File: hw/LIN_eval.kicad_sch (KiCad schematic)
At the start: 44 parts, among them J1 STM32 SWD, J2 Conn_01x03, Q2 DMG1012T, Q3 DMG1012T, Q4 DMG1012T, U1 TJA1029TK, U2 AP7370-33FDC, U3 STM32G030K8Tx, U4 DS18B20, Y2 8Mhz

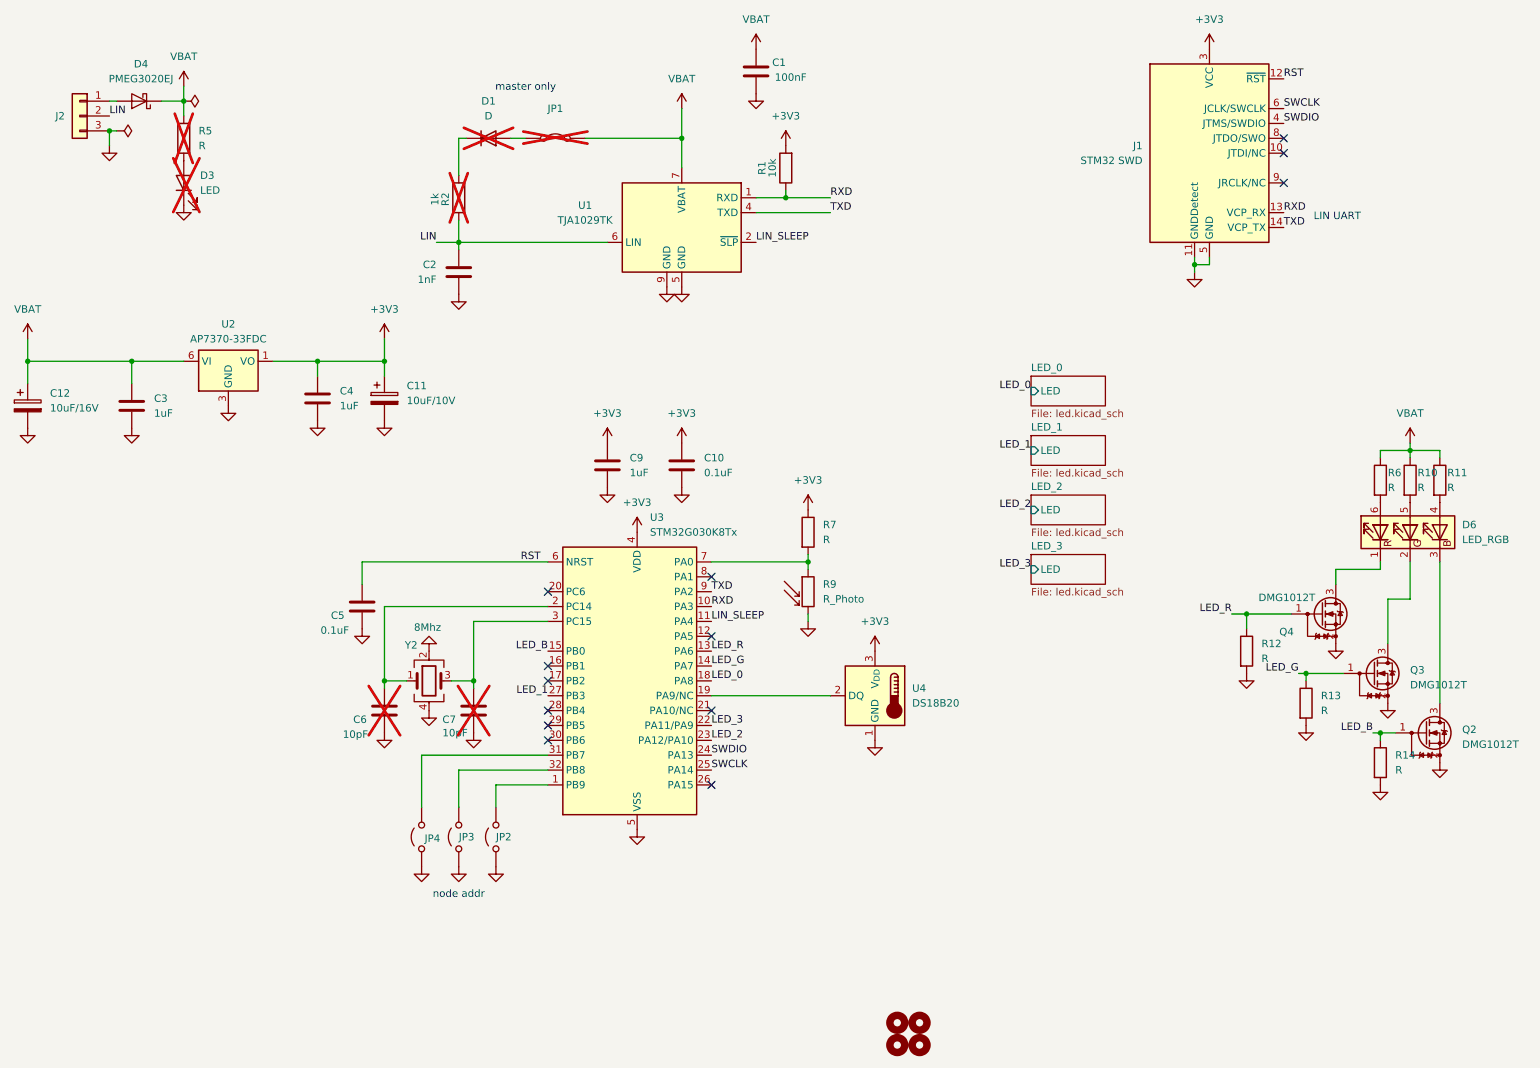
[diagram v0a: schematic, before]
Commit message: hw: version v2 with improvements
- removed LIN UART RX/TX from debugger connector as it drives signal from two sources
- added 5k pull-up to DS18B20 1-Wire bus
- added 1.27mm connector for additional devices on 1-Wire bus
- shifted address jumpers little bit farther from debugger connector
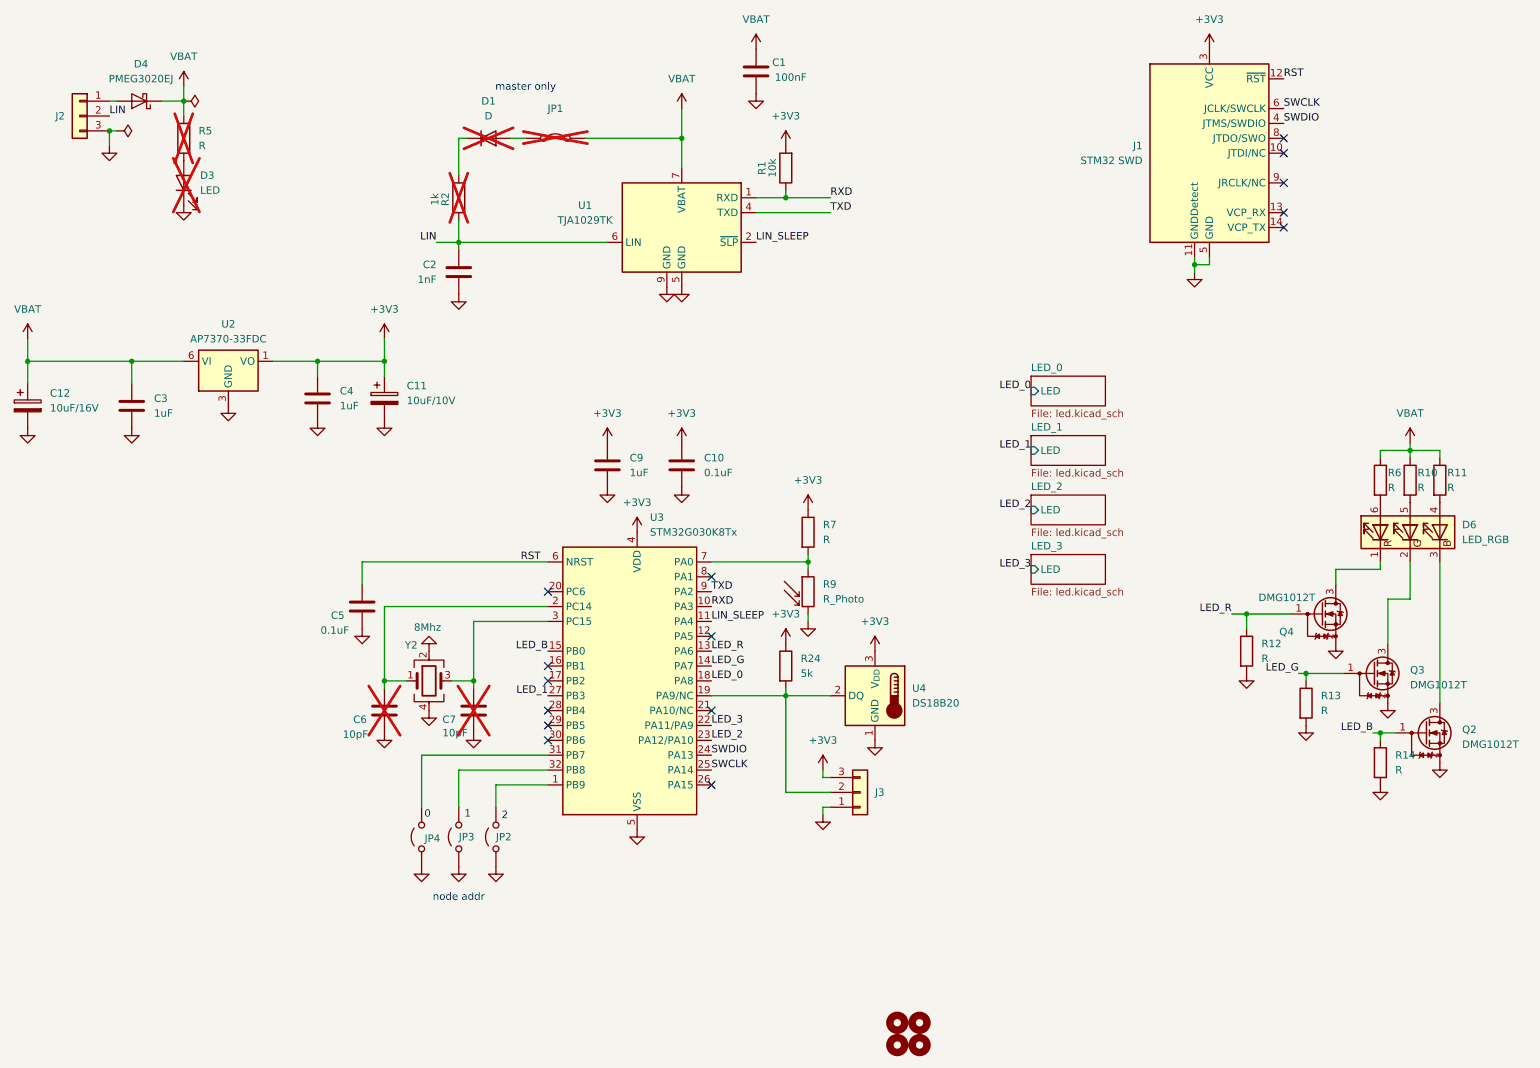
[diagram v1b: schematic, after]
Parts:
- added J3: Conn_01x03, Connector_PinHeader_1.27mm:PinHeader_1x03_P1.27mm_Vertical, symbol Connector_Generic:Conn_01x03
- added R24: 5k, Resistor_SMD:R_0805_2012Metric_Pad1.20x1.40mm_HandSolder, symbol Device:R
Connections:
- net +3V3: now also J3.3 (Pin_3), R24.1
- net GND: now also J3.1 (Pin_1)
- net RXD: no longer J1.13 (VCP_RX)
- net TXD: no longer J1.14 (VCP_TX)
- net at U3.19 (PA9/NC), U4.2 (DQ): now also J3.2 (Pin_2), R24.2
- no-connect marks 13 -> 15
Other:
- note added: "0"
- note added: "1"
- note added: "2"
- note removed: "LIN UART"
